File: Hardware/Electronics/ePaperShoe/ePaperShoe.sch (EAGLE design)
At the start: 20 parts, among them CN4 MicroUSB, U1 LM3671MF-3.3/NOPB, U3 MCP73871

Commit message: added circuit for driving screen
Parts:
- added C10: N.M., Nordic_nRF:CAPACITOR_0402_N
- added C11: 100pF, Nordic_nRF:CAPACITOR_0402_N
- added C12, C6, C9: 100nF, Nordic_nRF:CAPACITOR_0402_N
- added C13: 4.7�µF, Nordic_nRF:CAPACITOR_0603_N
- added C14: 1.0�µF, Nordic_nRF:CAPACITOR_0603_N
- added C15, C16, C3, C4: 12pF, Nordic_nRF:CAPACITOR_0402_N
- added C5: 0.8pF, Nordic_nRF:CAPACITOR_0402_N
- added FRAME2: FRAME-LETTER-MICHAELNO_PACKAGE, SparkFun-Aesthetics:FRAME-LETTER-MICHAELNO_PACKAGE
- added J2, J3, J4, J5: (no value), SparkFun-Connectors:CONN_01
- added J6: (no value), SparkFun-Connectors:CONN_04
- added L2: 3.9nH, Nordic_nRF:INDUCTOR_0402_N
- added R2: 1K, microbuilder:RESISTOR0805_NOOUTLINE
- added U2: NRF52832, Nordic_nRF:NRF52832
- added UC_LED: ORANGE, microbuilder:LED0805_NOOUTLINE
- added X1: 32MHz, Nordic_nRF:XTAL_32MHZ
- added X2: 32.768kHz, Nordic_nRF:XTAL_32KHZ
- FRAME1: value FRAME-LETTER-MICHAEL -> FRAME-LETTER-MICHAELNO_PACKAGE; device SparkFun-Aesthetics:FRAME-LETTER-MICHAEL -> SparkFun-Aesthetics:FRAME-LETTER-MICHAELNO_PACKAGE
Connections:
- new net ANT: C5.1, L2.1, U2.ANT@30
- new net DEC1: C6.1, U2.DEC1@01
- new net DEC2: C10.1, U2.DEC2@32
- new net DEC3: C11.1, U2.DEC3@33
- new net DEC4: C14.1, U2.DEC4@46
- new net N$15: R2.2, UC_LED.C
- new net N$3: C3.1, U2.XC2@35, X1.3
- new net P0.00/XL1: C15.2, U2.P0.00/XL1@02, X2.1
- new net P0.01: U2.P0.09/NFC1@11
- new net P0.01/XL2: C16.2, U2.P0.01/XL2@03, X2.2
- new net P0.02: U2.P0.02/AIN0@04
- new net P0.03: J6.4, U2.P0.03/AIN1@05
- new net P0.04: U2.P0.04/AIN2@06
- new net P0.05: U2.P0.05/AIN3@07
- new net P0.06: J6.3, U2.P0.06@08
- new net P0.07: J6.2, U2.P0.07@09
- new net P0.08: J6.1, U2.P0.08@10
- new net P0.09: U2.P0.10/NFC2@12
- new net P0.11: U2.P0.11@14, UC_LED.A
- new net P0.12: U2.P0.12@15
- new net P0.13: U2.P0.13@16
- new net P0.14: U2.P0.14@17
- new net P0.15: U2.P0.15@18
- new net P0.16: U2.P0.16@19
- new net P0.17: U2.P0.17@20
- new net P0.18/SWO: U2.P0.18/SWO@21
- new net P0.19: U2.P0.19@22
- new net P0.20: U2.P0.20@23
- new net P0.21/RESET: U2.P0.21/RESET@24
- new net P0.22: U2.P0.22@27
- new net P0.23: U2.P0.23@28
- new net P0.24: U2.P0.24@29
- new net P0.25: U2.P0.25@37
- new net P0.26: U2.P0.26@38
- new net P0.27: U2.P0.27@39
- new net P0.28: U2.P0.28@40
- new net P0.29: U2.P0.29@41
- new net P0.30: U2.P0.30@42
- new net P0.31: U2.P0.31@43
- new net RF: L2.2
- new net SWDCLK: U2.SWDCLK@25
- new net SWDIO: U2.SWDIO@26
- new net X1: C4.1, U2.XC1@34, X1.1
- net 3.3V: now also C12.1, C13.1, C9.1, J2.1, U2.VDD@13, U2.VDD@36, U2.VDD@48
- net GND: now also C10.2, C11.2, C12.2, C13.2, C14.2, C15.1, C16.1, C3.2, C4.2, C5.2, C6.2, C9.2, J5.1, R2.1, U2.VSS@31, U2.VSS@45, X1.2, X1.4
- net VBAT: now also J4.1
- net VBUS: now also J3.1
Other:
- note added: "Test points to check the various voltages"
- note added: "when populating the PCB"

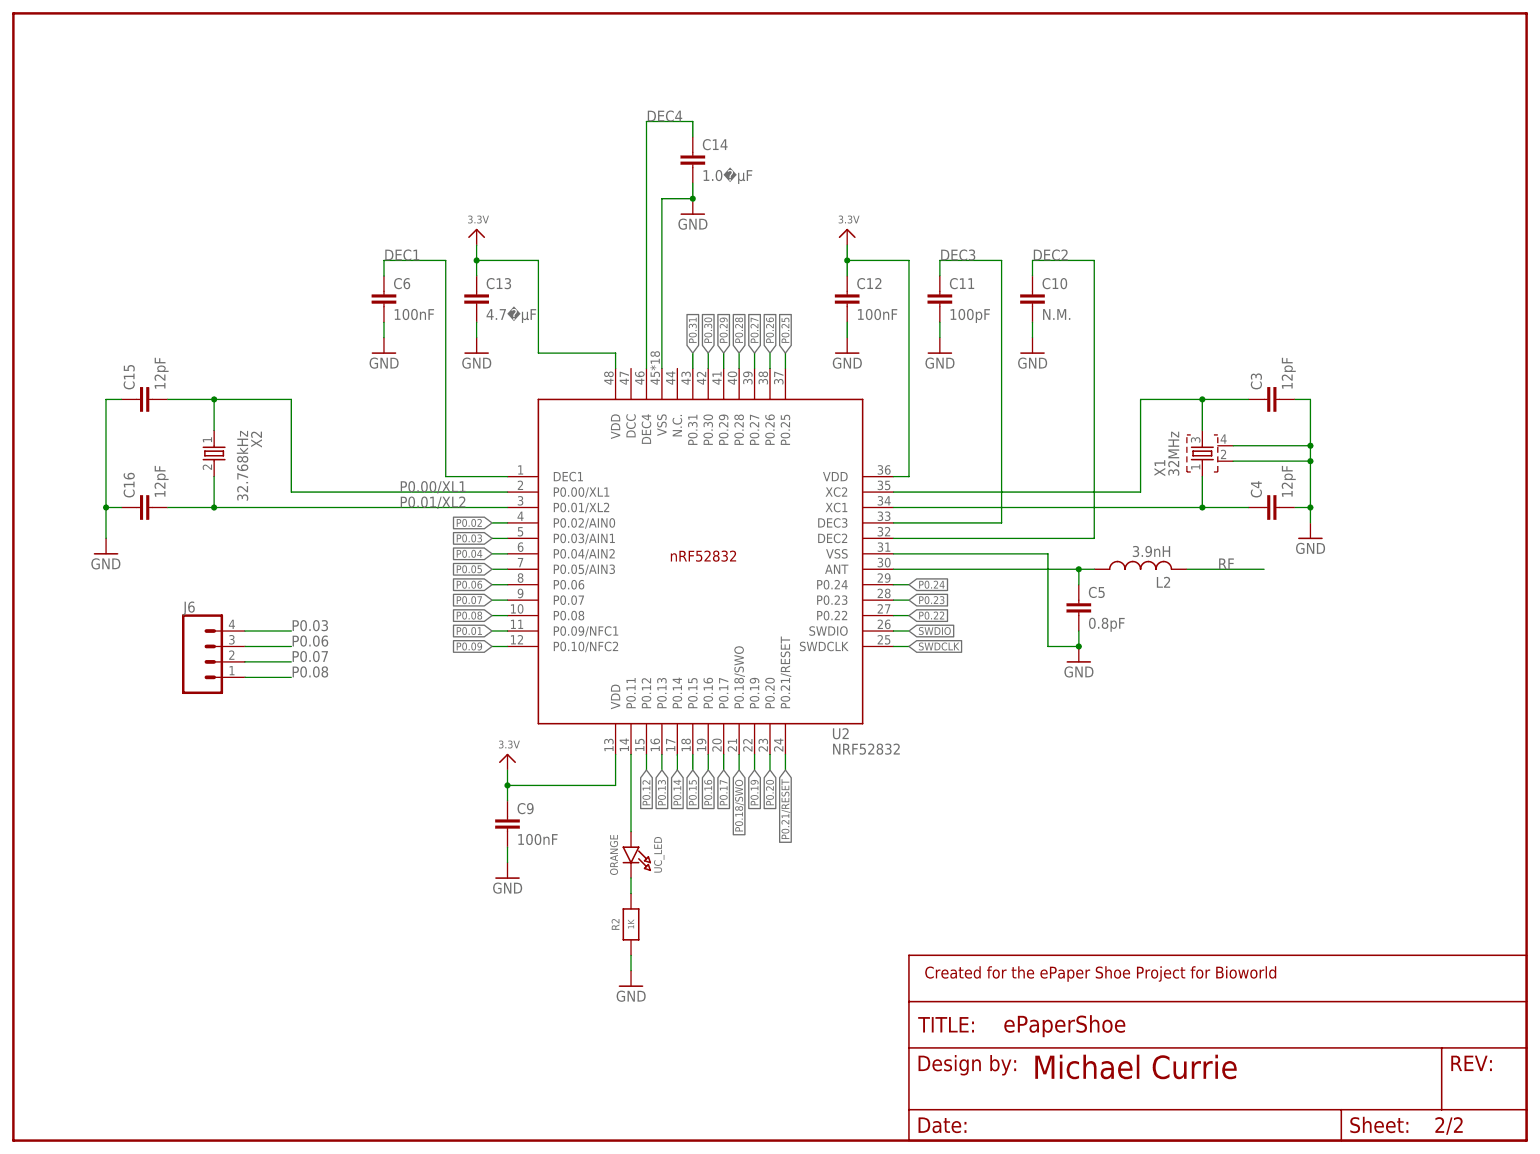
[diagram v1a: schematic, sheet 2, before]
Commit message: Changes made to the screen circuit
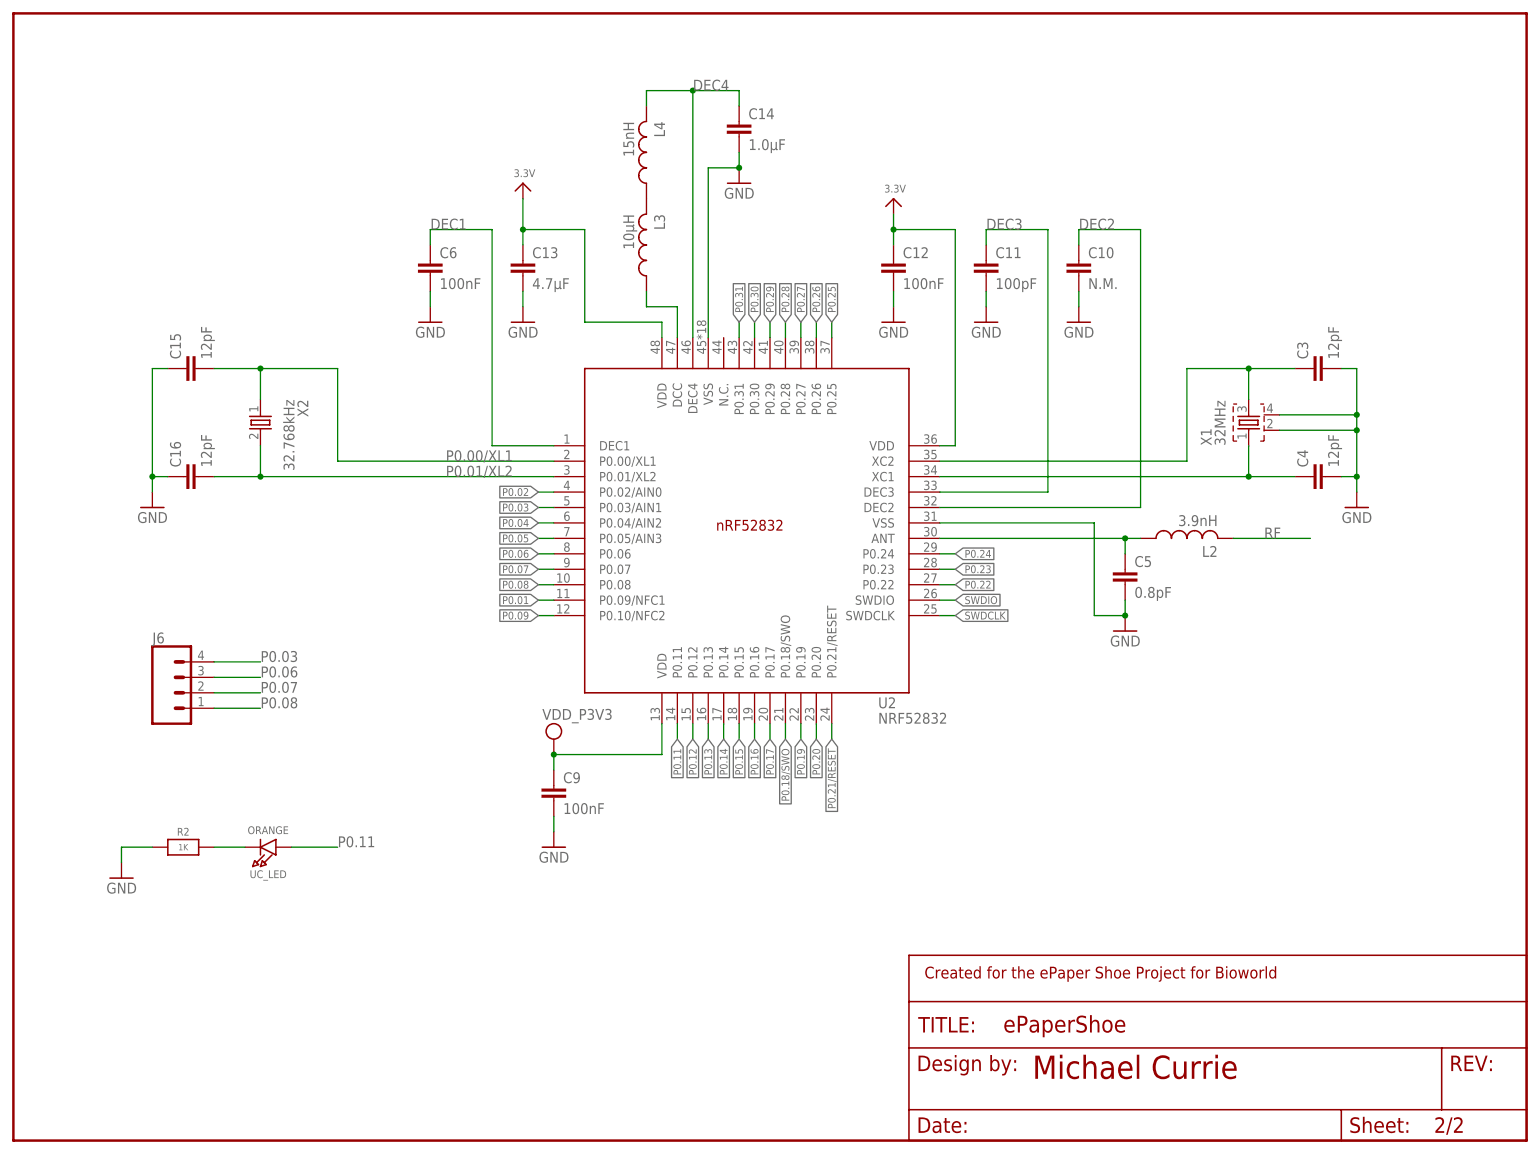
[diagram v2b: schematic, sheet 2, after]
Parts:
- added L3: 10µH, Nordic_nRF:INDUCTOR_0603_N
- added L4: 15nH, Nordic_nRF:INDUCTOR_0402_N
- C13: value 4.7�µF -> 4.7µF
- C14: value 1.0�µF -> 1.0µF
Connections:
- new net N$4: L3.2, L4.1
- new net N$5: L3.1, U2.DCC@47
- new net VDD_P3V3: C9.1, U2.VDD@13
- net 3.3V: no longer C9.1, U2.VDD@13
- net DEC4: now also L4.2
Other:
- note added: "Can be used as a battery"
- note added: "low voltage indicator."
- moved on the sheet: C10, C11, C12, C13, C14, C15, C16, C3, C4, C5, C6, C9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
